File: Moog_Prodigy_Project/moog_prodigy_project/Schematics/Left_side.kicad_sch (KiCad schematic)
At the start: 86 parts, among them Q1 CA3046, Q14 BF244A, Q15 BC549, Q2 CA3046, Q4 CA3046, Q6 BC549, U1 LM393BIPWR, U11 +12V, U12 +12V, U15 +12V, U16 +12V, U17 +12V, U18 +12V, U19 +12V, U20 +12V, U21 +12V, U2A OPA134, U2B OPA134, U3 +12V, U4 +12V, U41 +12V, U5 NE5532, U55 -12V, U56 -12V, U57 -12V, U58 -12V, U59 -12V, U6 LM393BIPWR, U60 -12V, U61 -12V, U62 -12V, U63 -12V, U64 +12V, U65 +12V, U66 -12V, U7 AD8066ARM, U8 NE5532

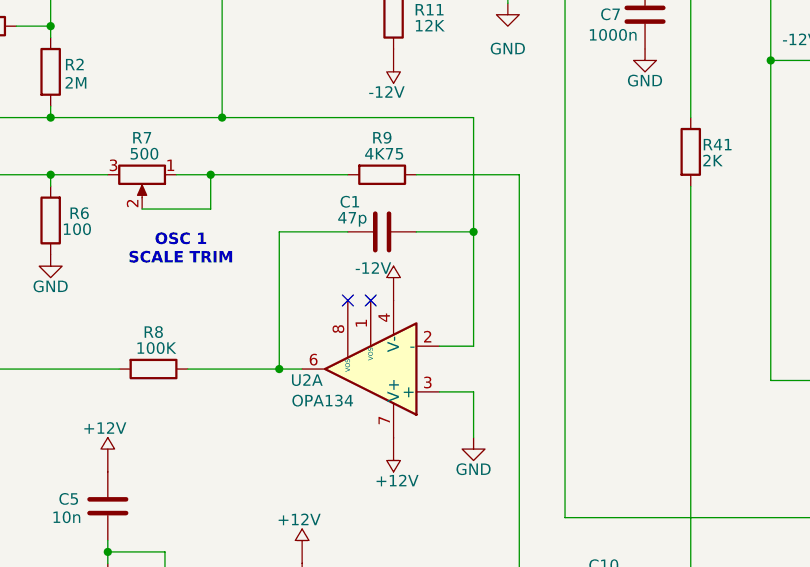
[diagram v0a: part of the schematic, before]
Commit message: Vcc fix, banana jack, connector, OP adding top sch
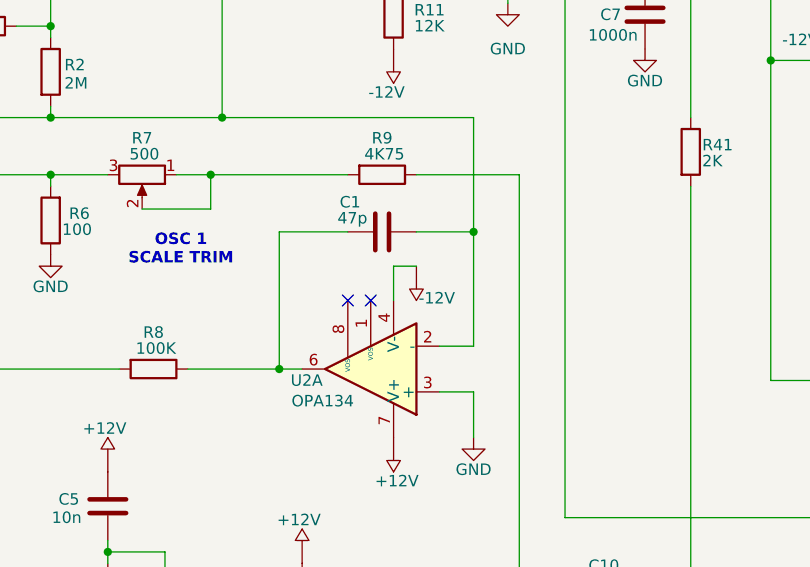
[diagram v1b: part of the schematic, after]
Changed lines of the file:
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@@
 	(wire
 		(pts
+			(xy 113.03 71.12) (xy 110.49 71.12)
+		)
+		(stroke
+			(width 0)
+			(type default)
+		)
+	)
+	(wire
+		(pts
 			(xy 44.45 142.24) (xy 58.42 142.24)
 		)
@@
 	(wire
 		(pts
+			(xy 110.49 71.12) (xy 110.49 74.93)
+		)
+		(stroke
+			(width 0)
+			(type default)
+		)
+	)
+	(wire
+		(pts
 			(xy 189.23 49.53) (xy 189.23 58.42)
 		)
@@
 	(symbol
 		(lib_id "Power_supply:Vcc_reference")
-		(at 110.49 73.66 0)
+		(at 113.03 72.39 180)
 		(unit 1)
 		(exclude_from_sim no)
@@
 		(dnp no)
 		(property "Reference" "U62"
-			(at 106.68 73.0251 0)
+			(at 116.84 73.0249 0)
 			(effects
 				(font
@@
 		)
 		(property "Value" "-12V"
-			(at 110.236 71.374 0)
+			(at 113.284 74.676 0)
 			(effects
 				(font
@@
 		)
 		(property "Footprint" ""
-			(at 110.49 73.66 0)
+			(at 113.03 72.39 0)
 			(effects
 				(font
@@
 		)
 		(property "Datasheet" ""
-			(at 110.49 73.66 0)
+			(at 113.03 72.39 0)
 			(effects
 				(font
@@
 		)
 		(property "Description" ""
-			(at 110.49 73.66 0)
+			(at 113.03 72.39 0)
 			(effects
 				(font

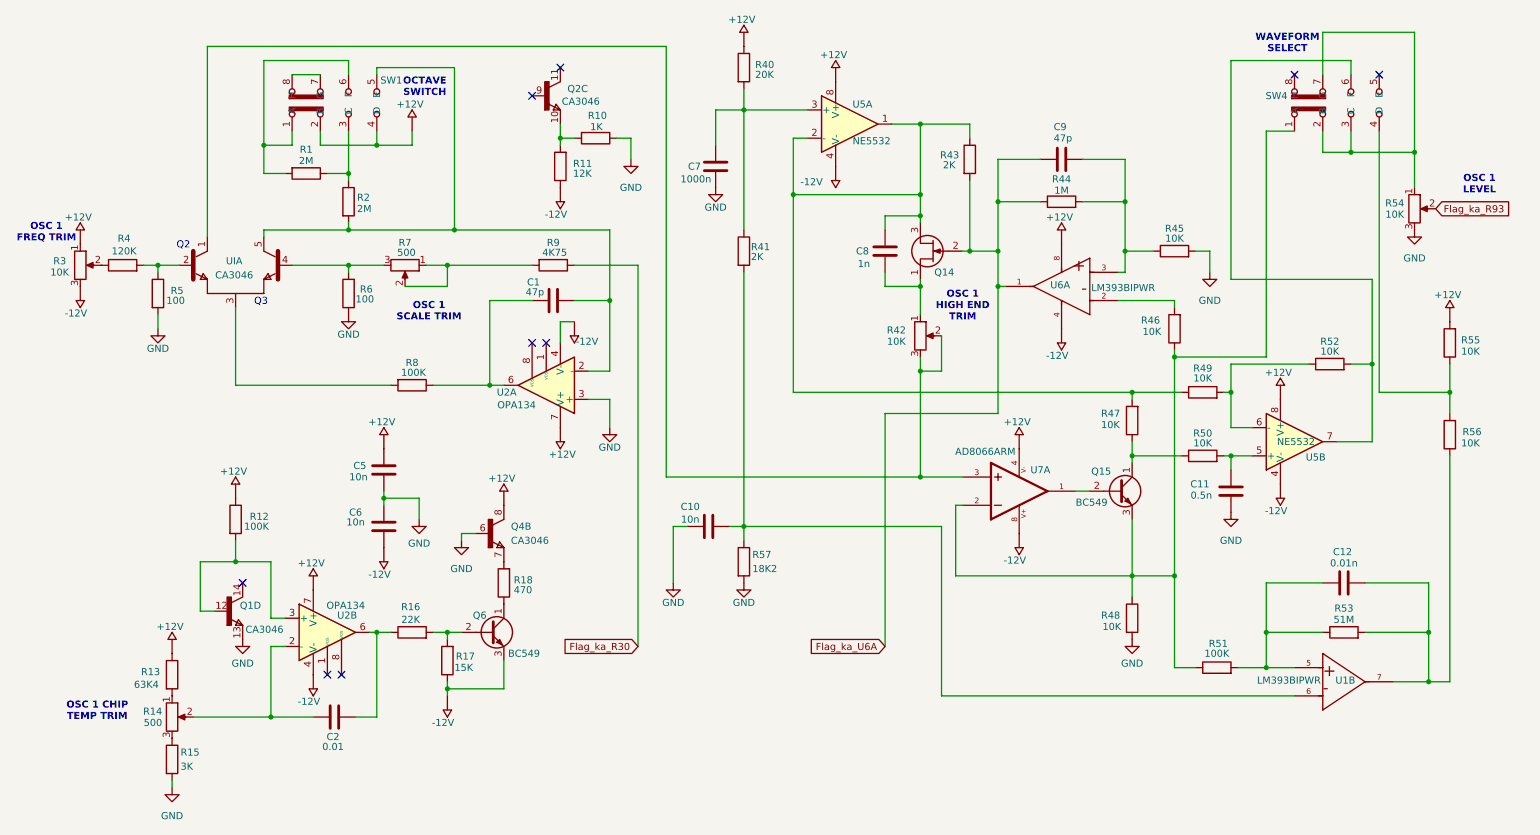
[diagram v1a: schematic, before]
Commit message: 4007 update, impor biblioteka LM 393
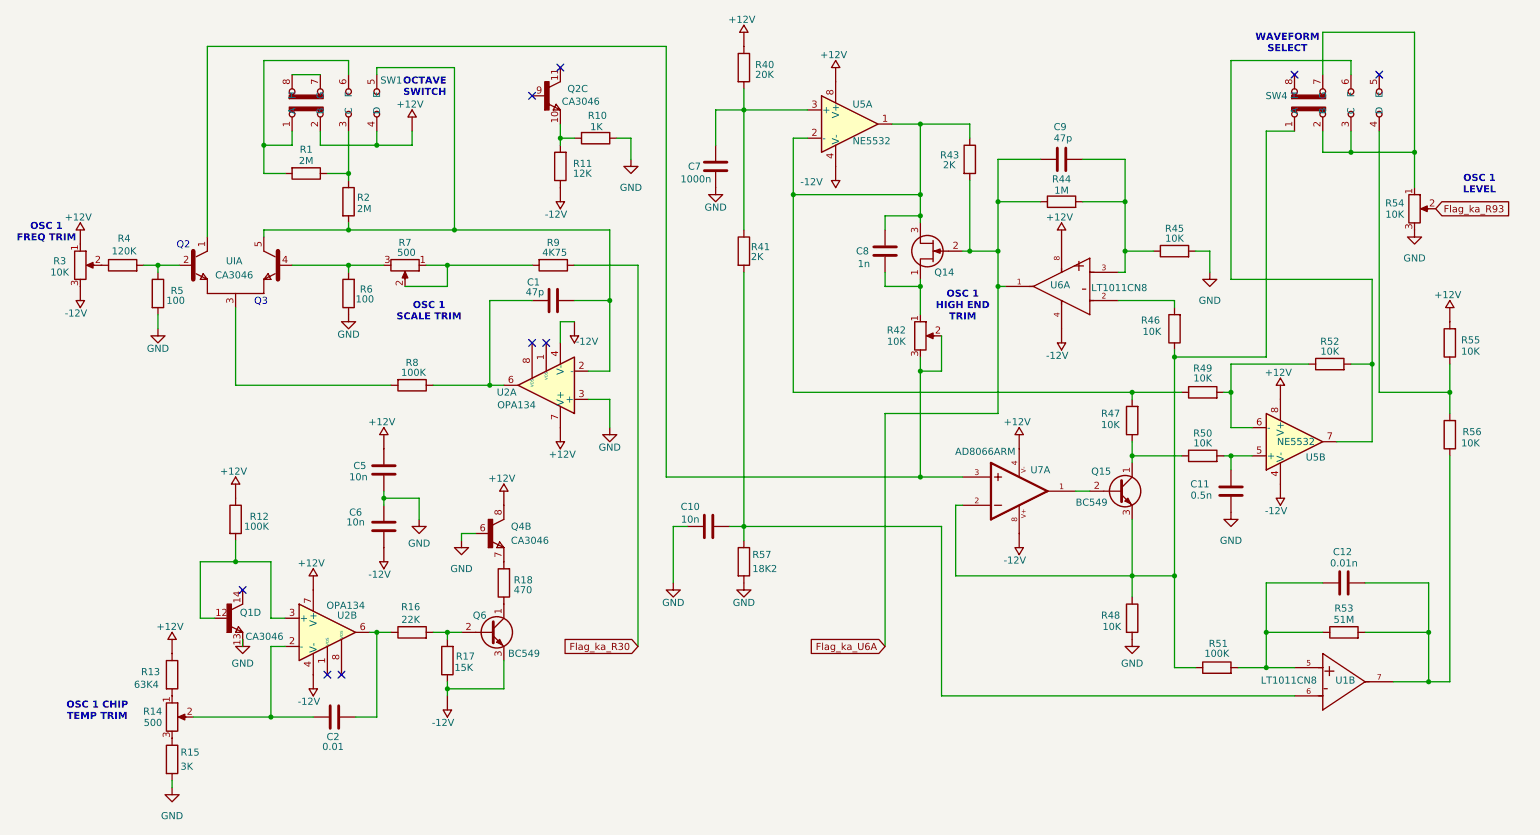
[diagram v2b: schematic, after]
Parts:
- U1, U6: value LM393BIPWR -> LT1011CN8; footprint (none) -> Package_DIP:DIP-8_W7.62mm_Socket
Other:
- moved on the sheet: Q1D
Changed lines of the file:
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@@
 	)
 	(no_connect
-		(at 53.34 118.11)
+		(at 53.34 119.38)
 	)
 	(no_connect
@@
 	(wire
 		(pts
-			(xy 45.72 123.19) (xy 48.26 123.19)
+			(xy 45.72 124.46) (xy 48.26 124.46)
 		)
 		(stroke
@@
 	(wire
 		(pts
+			(xy 53.34 129.54) (xy 53.34 128.27)
+		)
+		(stroke
+			(width 0)
+			(type default)
+		)
+	)
+	(wire
+		(pts
 			(xy 76.2 127) (xy 77.47 127)
 		)
@@
 	(wire
 		(pts
-			(xy 45.72 114.3) (xy 45.72 123.19)
+			(xy 45.72 114.3) (xy 45.72 124.46)
 		)
 		(stroke
@@
 			)
 		)
-		(property "Value" "LM393BIPWR"
+		(property "Value" "LT1011CN8"
 			(at 205.994 65.024 0)
 			(effects
@@
 			)
 		)
-		(property "Footprint" ""
+		(property "Footprint" "Package_DIP:DIP-8_W7.62mm_Socket"
 			(at 210.82 62.23 0)
 			(effects
@@
 		(lib_name "CA3046_3")
 		(lib_id "CA3046:CA3046")
-		(at 50.8 123.19 0)
+		(at 50.8 124.46 0)
 		(unit 4)
 		(exclude_from_sim no)
@@
 		(dnp no)
 		(property "Reference" "Q1"
-			(at 52.832 122.174 0)
+			(at 52.832 123.444 0)
 			(effects
 				(font
@@
 		)
 		(property "Value" "CA3046"
-			(at 53.848 126.492 0)
+			(at 53.848 127.762 0)
 			(effects
 				(font
@@
 		)
 		(property "Footprint" ""
-			(at 50.8 123.19 0)
+			(at 50.8 124.46 0)
 			(effects
 				(font
@@
 		)
 		(property "Datasheet" ""
-			(at 50.8 123.19 0)
+			(at 50.8 124.46 0)
 			(effects
 				(font
@@
 		)
 		(property "Description" ""
-			(at 50.8 123.19 0)
+			(at 50.8 124.46 0)
 			(effects
 				(font
@@
 		)
 		(property "MF" "ON Semiconductor / Fairchild"
-			(at 50.8 123.19 0)
+			(at 50.8 124.46 0)
 			(effects
 				(font
@@
 		)
 		(property "Description_1" "RF Transistor 5 NPN 15V 50mA 550MHz 300mW Through Hole 14-PDIP"
-			(at 50.8 123.19 0)
+			(at 50.8 124.46 0)
 			(effects
 				(font
@@
 		)
 		(property "Package" "None"
-			(at 50.8 123.19 0)
+			(at 50.8 124.46 0)
 			(effects
 				(font
@@
 		)
 		(property "Price" "None"
-			(at 50.8 123.19 0)
+			(at 50.8 124.46 0)
 			(effects
 				(font
@@
 		)
 		(property "SnapEDA_Link" "https://www.snapeda.com/parts/CA3046/Onsemi/view-part/?ref=snap"
-			(at 50.8 123.19 0)
+			(at 50.8 124.46 0)
 			(effects
 				(font
@@
 		)
 		(property "MP" "CA3046"
-			(at 50.8 123.19 0)
+			(at 50.8 124.46 0)
 			(effects
 				(font
@@
 		)
 		(property "Availability" "Not in stock"
-			(at 50.8 123.19 0)
+			(at 50.8 124.46 0)
 			(effects
 				(font
@@
 		)
 		(property "Check_prices" "https://www.snapeda.com/parts/CA3046/Onsemi/view-part/?ref=eda"
-			(at 50.8 123.19 0)
+			(at 50.8 124.46 0)
 			(effects
 				(font
@@
 			)
 		)
-		(property "Value" "LM393BIPWR"
+		(property "Value" "LT1011CN8"
 			(at 241.554 135.636 0)
 			(effects
@@
 			)
 		)
-		(property "Footprint" ""
+		(property "Footprint" "Package_DIP:DIP-8_W7.62mm_Socket"
 			(at 242.57 133.35 0)
 			(effects

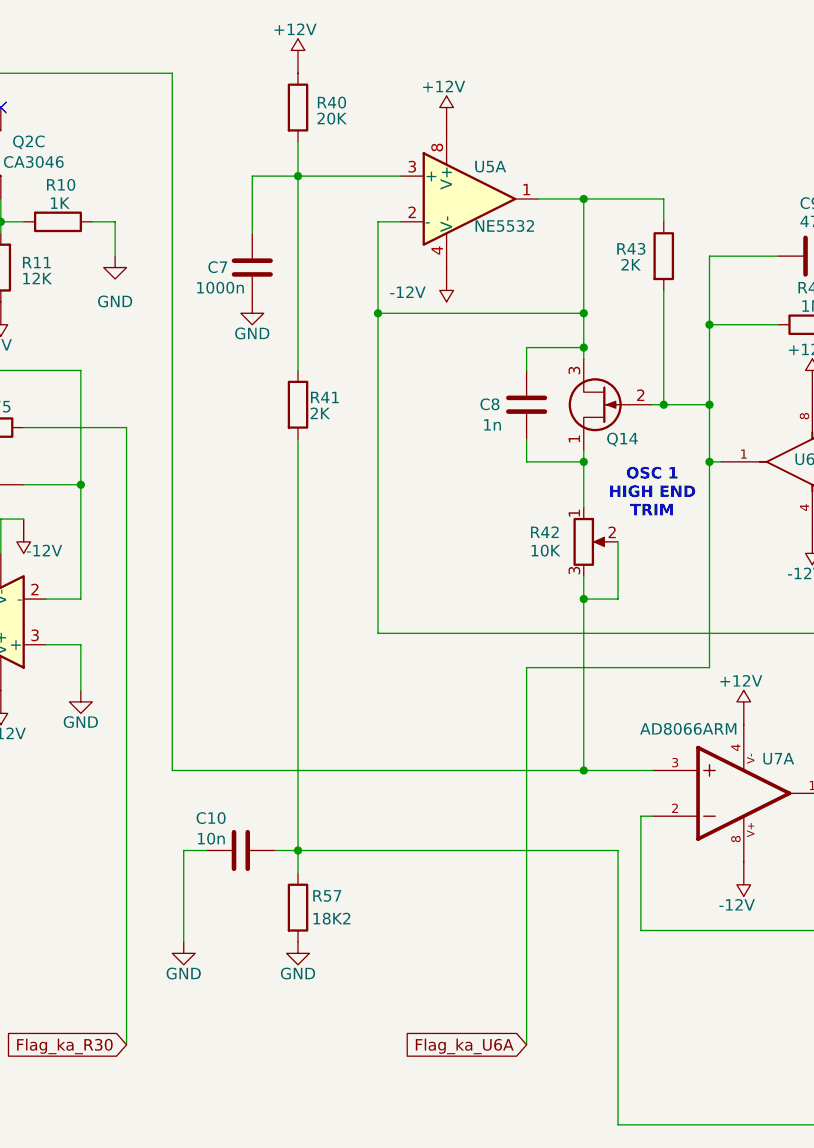
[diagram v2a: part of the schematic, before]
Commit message: Zamena fet-ova E112 sa BF256C + update dokumentacije
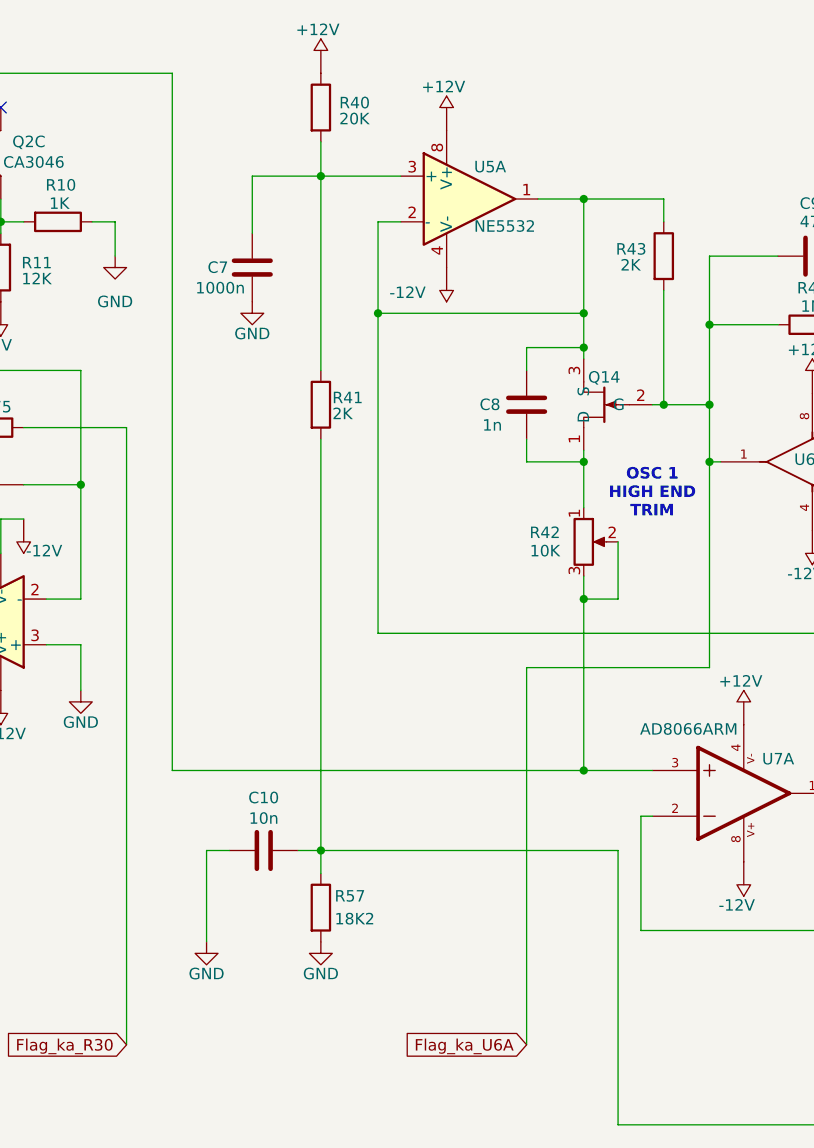
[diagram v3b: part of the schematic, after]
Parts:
- removed Q14: BF244A, Package_TO_SOT_THT:TO-92_Inline, symbol Transistor_FET:BF244A
- added Q14: ~, BF256C:TO92127P478H483-3, symbol Transistor_FET:BF256C
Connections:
- net Flag_ka_U6A: now also Q14.2 (G)
- net at C8.2, R43.1, R47.2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: now also Q14.3 (S)
- net at C8.1, R42.1: now also Q14.1 (D)
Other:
- moved on the sheet: C10, R40, R41, R57

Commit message: New update footprints
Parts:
- renumbered U2A to U2A1, U2B to U2B3, U1 to U6, UI to UI2
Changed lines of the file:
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@@
 		(on_board yes)
 		(dnp no)
-		(property "Reference" "U2A"
+		(property "Reference" "U2A1"
 			(at 100.838 83.82 0)
 			(effects
@@
 			(project "moog_prodigy_project"
 				(path "/db469bdb-b6c3-4a16-9199-d4e6b8d556e8/2ede1db1-77b0-45c3-aa08-ac2fbfd2e808"
-					(reference "U2A")
+					(reference "U2A1")
 					(unit 1)
 				)
@@
 		(on_board yes)
 		(dnp no)
-		(property "Reference" "U2B"
+		(property "Reference" "U2B3"
 			(at 72.136 123.952 0)
 			(effects
@@
 			(project "moog_prodigy_project"
 				(path "/db469bdb-b6c3-4a16-9199-d4e6b8d556e8/2ede1db1-77b0-45c3-aa08-ac2fbfd2e808"
-					(reference "U2B")
+					(reference "U2B3")
 					(unit 1)
 				)
@@
 		(on_board yes)
 		(dnp no)
-		(property "Reference" "U1"
+		(property "Reference" "U6"
 			(at 251.714 135.636 0)
 			(effects
@@
 			(project ""
 				(path "/db469bdb-b6c3-4a16-9199-d4e6b8d556e8/2ede1db1-77b0-45c3-aa08-ac2fbfd2e808"
-					(reference "U1")
+					(reference "U6")
 					(unit 2)
 				)
@@
 		(on_board yes)
 		(dnp no)
-		(property "Reference" "UI"
+		(property "Reference" "UI2"
 			(at 51.816 60.198 0)
 			(effects
@@
 			(project ""
 				(path "/db469bdb-b6c3-4a16-9199-d4e6b8d556e8/2ede1db1-77b0-45c3-aa08-ac2fbfd2e808"
-					(reference "UI")
+					(reference "UI2")
 					(unit 1)
 				)

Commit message: Footpring fix 2
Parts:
- UI2: footprint (none) -> CA3046:DIL14
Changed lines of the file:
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@@
 			)
 		)
-		(property "Footprint" ""
+		(property "Footprint" "CA3046:DIL14"
 			(at 52.07 60.96 0)
 			(effects
